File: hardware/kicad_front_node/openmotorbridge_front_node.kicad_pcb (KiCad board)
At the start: 2 copper layers, 82 x 50 mm, 58 parts, among them J1 12V_KL15_GND, J10 12V_QI_POWER, J11 12V_AUX_LIGHT, J12 QWIIC_I2C, J2 CAN_H_L_GND, J3 HANDLEBAR_MULTI_BTN, J4 USB_UPSTREAM_HOST, J5 USB_DN1_PHONE_PD20W, J5_MP3 USB_DN3_GLOVEBOX_PD20W, J6 USB_DN2_CP2AA_PIGTAIL, J6_AUX USB_DN4_COCKPIT_AUX, J7 USB-C_SERVICE, J8 ACTION_CAM_5V_PWR, J9 MIRROR_BSD_LEDS, K1 CPC1017N_CAN_RELAY, Q1 DMN63D8_BSD_MOSFET, Q2 TPS1H100_AUX_LIGHT, SW1 BOOT, SW2 RESET, U1 ESP32-S3-WROOM-1U, U2 USB2514Bi-AEZG, U3 TPS54302_5V_BUCK, U4 TPS2051B_PORT2_GATE, U5 SW3526_USB_PD1_20W, U6 TCAN334G_CAN, U7 TLV75533P_3V3_LDO, U8 SW3526_USB_PD3_20W, U9 DW3110, Y1 24.000MHz

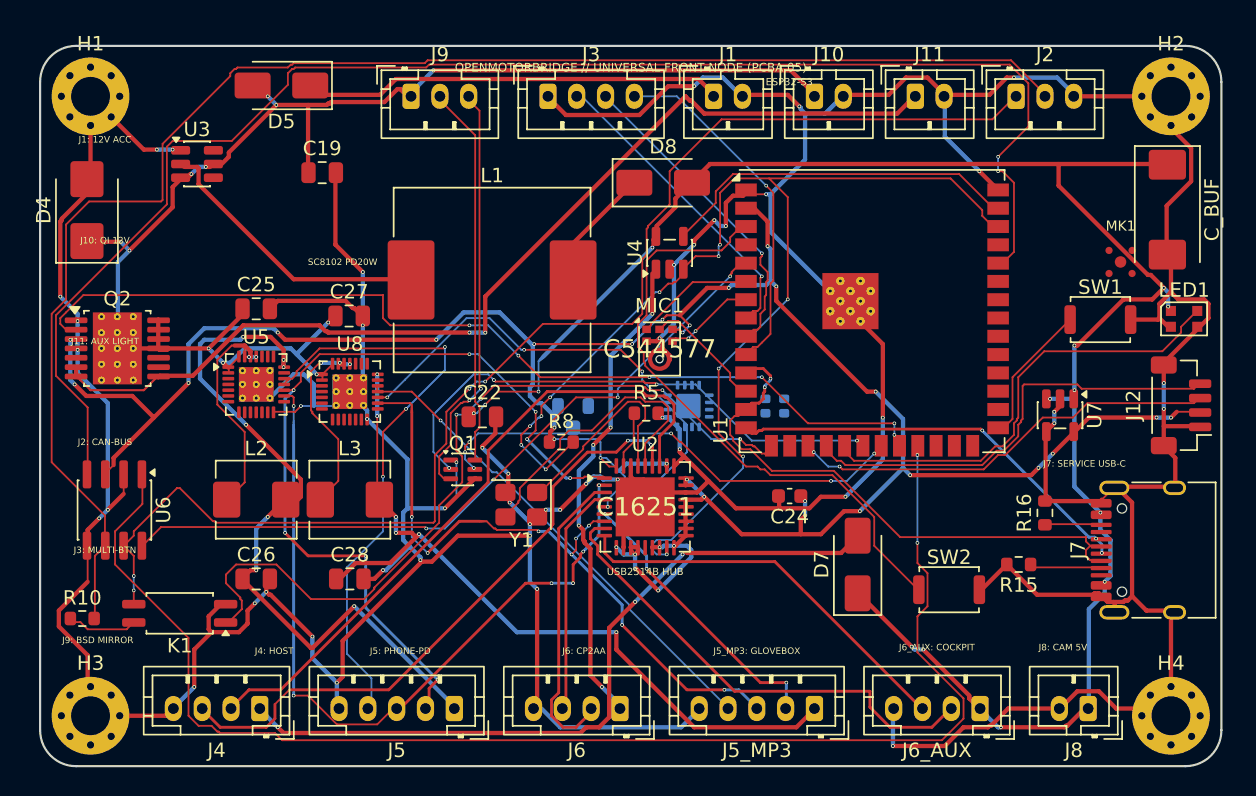
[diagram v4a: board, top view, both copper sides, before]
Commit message: feat(audio): genuinely integrate Qualcomm QCC3084 BT 5.4 Audio SoC for dual-helmet aptX HD link
- Hardware (PCBA 01): Placed U9 (Qualcomm QCC3084 module with onboard ceramic antenna) at (175, 106) on F.Cu; wired I2S bus, UART, and reset/enable controls in mcu_codec_can.kicad_sch.
- Firmware: Upgraded bluetooth_audio_manager to full QCC3084 driver supporting Dual-A2DP aptX HD/Adaptive, LE Audio Auracast, independent AVRCP volume, and modal HFP 1.8 telephony interceptor.
- Docs: Updated 02_intercom_matrix_profiles, 07_pcba_hardware_pinouts, and 09_firmware_architecture with technical specs and pinout tables for the dedicated Qualcomm audio link.
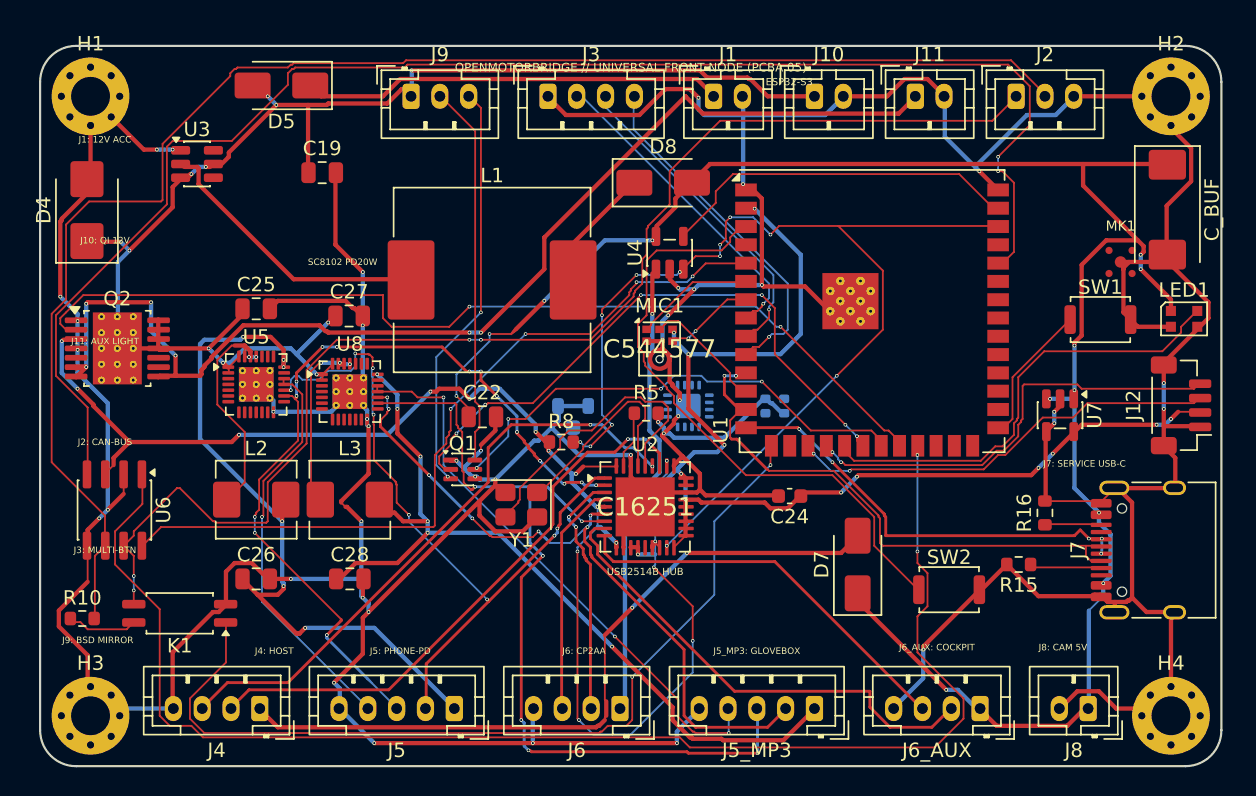
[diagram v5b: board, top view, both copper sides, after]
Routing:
- net USB_DN1_CC: track 41.1 -> 28.1 mm, vias 3 -> 1
- net USB_DN3_DP: track 48.1 -> 60.9 mm, vias 8 -> 6
- net OTTOCAST_FAULT_N: track 85.1 -> 73.8 mm
- net +12V_AUX: track 70.9 -> 79.6 mm, vias 2 -> 6
- net USB_DN3_DM: track 56.0 -> 47.5 mm, vias 6 -> 7
- net USB_DN1_DM: track 58.7 -> 50.3 mm
- net VCC_3V3: track 178.3 -> 185.6 mm, vias 35 -> 29
- net CAN_TERM_EN: track 55.3 -> 62.3 mm, vias 4 -> 2
- net USB_UP_DM: track 46.3 -> 40.5 mm, vias 0 -> 2
- net USB_DN3_CC: track 34.2 -> 39.8 mm, vias 1 -> 3
- net GND: track 447.4 -> 441.8 mm, vias 49 -> 42
- net BSD_LED_LEFT: track 37.4 -> 42.2 mm, vias 4 -> 6
- net USB_DN1_DP: track 53.3 -> 58.0 mm, vias 6 -> 15
- net USB_DN2_DM: track 21.3 -> 17.2 mm, vias 0 -> 2
- net CAN_SILENT: track 50.6 -> 54.4 mm
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
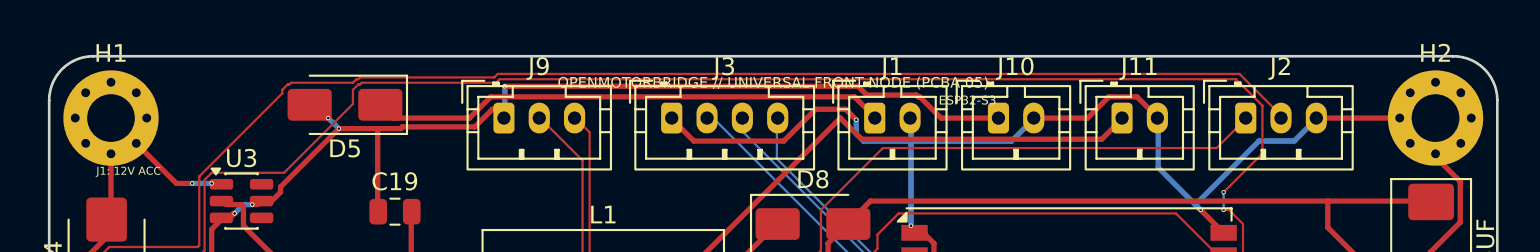
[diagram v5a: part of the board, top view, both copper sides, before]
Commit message: feat(system): architecture refinement v6 across hardware, firmware and docs
- Hardware:
  * PCBA 09 (OMM 2.4 GHz Intercom): Upgrade to Everest Semi ES8388 stereo codec (QFN-28)
    and Multi-Use USB-C connector (J1) combining power, WebUSB flashing and stereo audio.
  * PCBA 08 (Radar 2.0 Sub-MCU): Strict HF hardening (2x U.FL: 6.5 GHz UWB & 5.9 GHz V2X;
    no 2.4 GHz/BLE at rear), right-angle 4-pin flashing header J3.
  * PCBA 03 (Cartridge): 8-pin Kelvin-grounded audio/power header with isolated PGND/AGND.
  * CAD: Standardize DIN 934 hex nut pockets across module enclosures.

- Firmware:
  * UWB Backbone: Add multi-channel substream audio downlink (sub-channels 0/1 music,
    sub-channel 2 voice) and audio uplink packet definitions.
  * Smart Cartridge: Implement zero-latency (<1 ms) voice routing to intercom mic pin,
    A2DP music stream buffering for mesh group sharing, and 100 Hz upstream audio capture.
  * Central Box: Central DSP mixer ducking (-18 dB), voice activity detection (VAD), and
    multi-channel UWB dispatching.
  * OMM Module: Implement ES8388 stereo codec driver and I2S master duplex stream.
  * Radar Sub-MCU: Confirm 2.4 GHz RF disable and autonomous emergency strobe trigger (<1 ms).

- Documentation & WebApp:
  * Align DE & EN chapters (01, 02, 03, 04b, 07, 08, 14, 15, 16) with v6 specifications.
  * Update WebApp PWA System Builder with ES8388 stereo codec and OMM 446 PMR/DMR module.
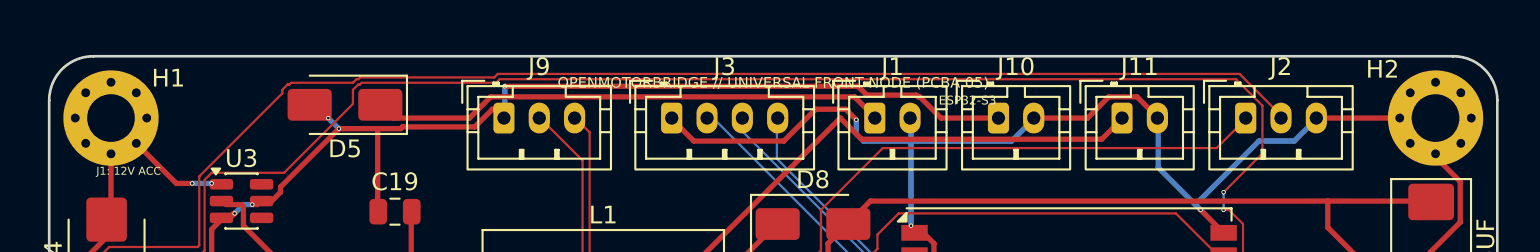
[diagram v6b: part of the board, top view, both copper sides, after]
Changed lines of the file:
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@@
 		(tags "mountinghole M2.5")
 		(property "Reference" "H2"
-			(at 0 -3.65 0)
+			(at -3 -2.75 0)
 			(layer "F.SilkS")
 			(effects
@@
 		(tags "mountinghole M2.5")
 		(property "Reference" "H1"
-			(at 0 -3.65 0)
-			(layer "F.SilkS")
-			(effects
+			(at 3.25 -2.25 0)
+			(layer "F.SilkS")
+			(effects

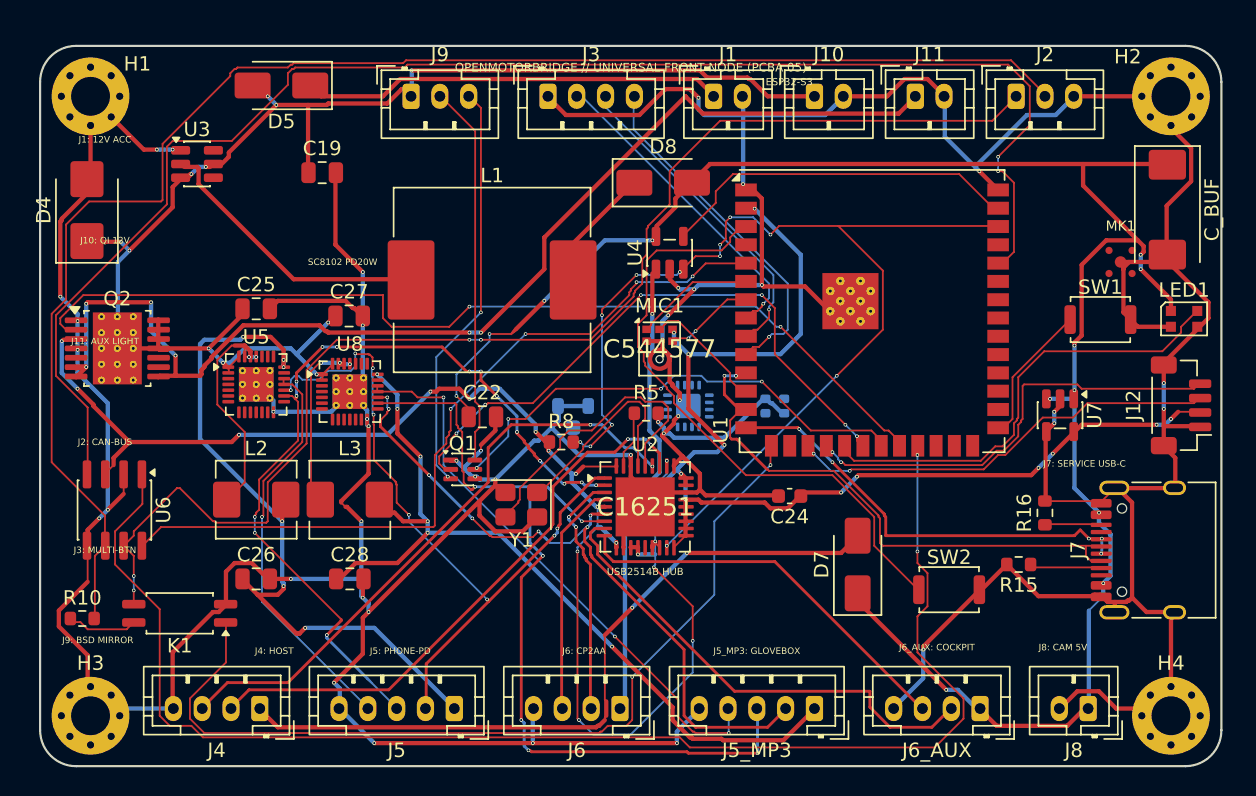
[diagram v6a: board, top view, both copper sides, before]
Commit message: fix(pcb): shift MK1 microphone on PCBA 05 Front-Node for 3D clearance against C_BUF and re-render 3D views
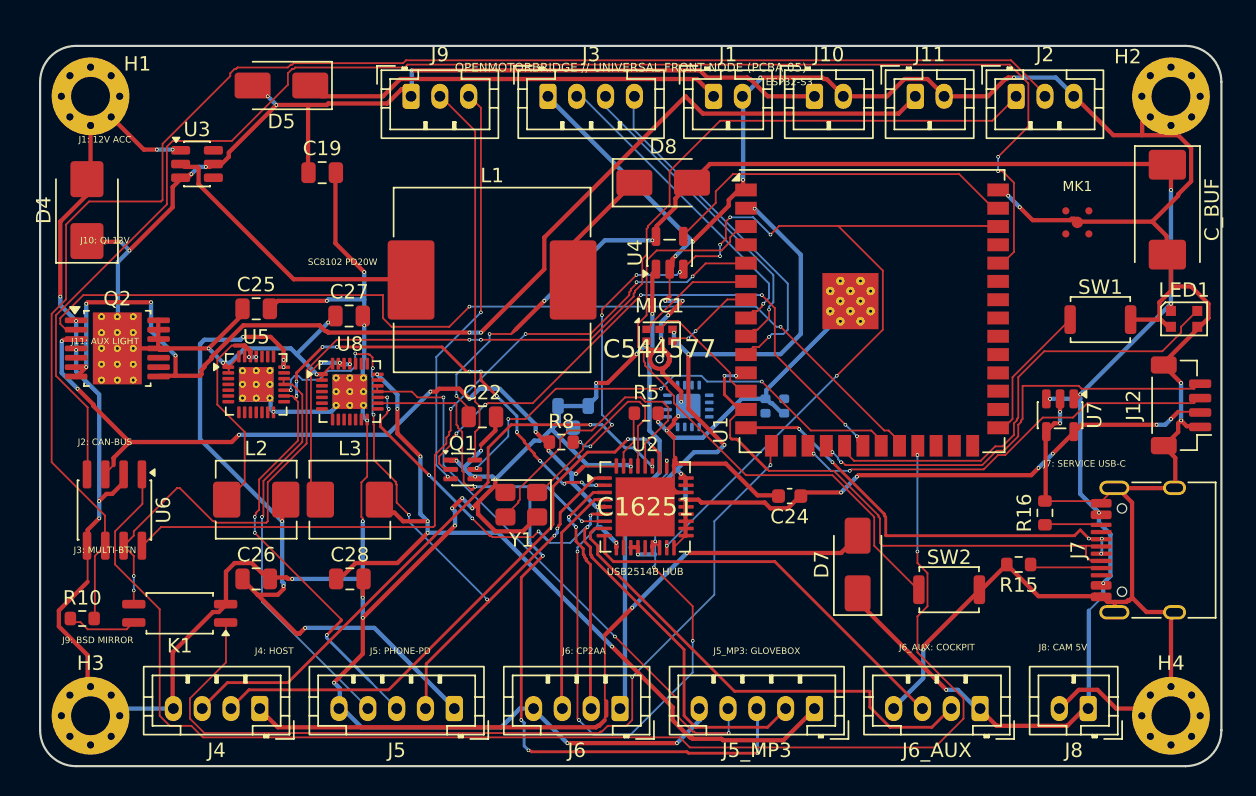
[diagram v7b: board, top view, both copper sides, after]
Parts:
- moved MK1 4.07 mm to (172.0, 82.2)
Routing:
- net VCC_5V: track 133.7 -> 123.8 mm, vias 12 -> 11
- net GND: track 441.8 -> 448.2 mm, vias 42 -> 51
- net +12V_PROT: track 100.6 -> 95.9 mm
- net VBUS_BUCK_OUT: track 8.54 -> 5.94 mm
- net USB_SERV_DM: track 39.3 -> 37.4 mm
- net VCC_3V3: track 185.6 -> 183.8 mm
- net KL15_12V_SW: track 29.4 -> 28.3 mm
- net AUX_LIGHT_EN: track 67.3 -> 66.3 mm
- net SW_PD3_BUCK: track 13.0 -> 12.0 mm
- net PTT_IN2_N: track 21.8 -> 21.1 mm
- net TWAI_TX: track 97.3 -> 96.6 mm
- net VCC_5V_OTTOCAST: track 32.2 -> 31.6 mm
- net BSD_LED_RIGHT: track 33.9 -> 33.3 mm
